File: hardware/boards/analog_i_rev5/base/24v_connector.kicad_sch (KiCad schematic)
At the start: 16 parts, among them IC8001 INA826AIDR, J8001 Barrel_Jack PJ-202BH, U4001 INA181A2

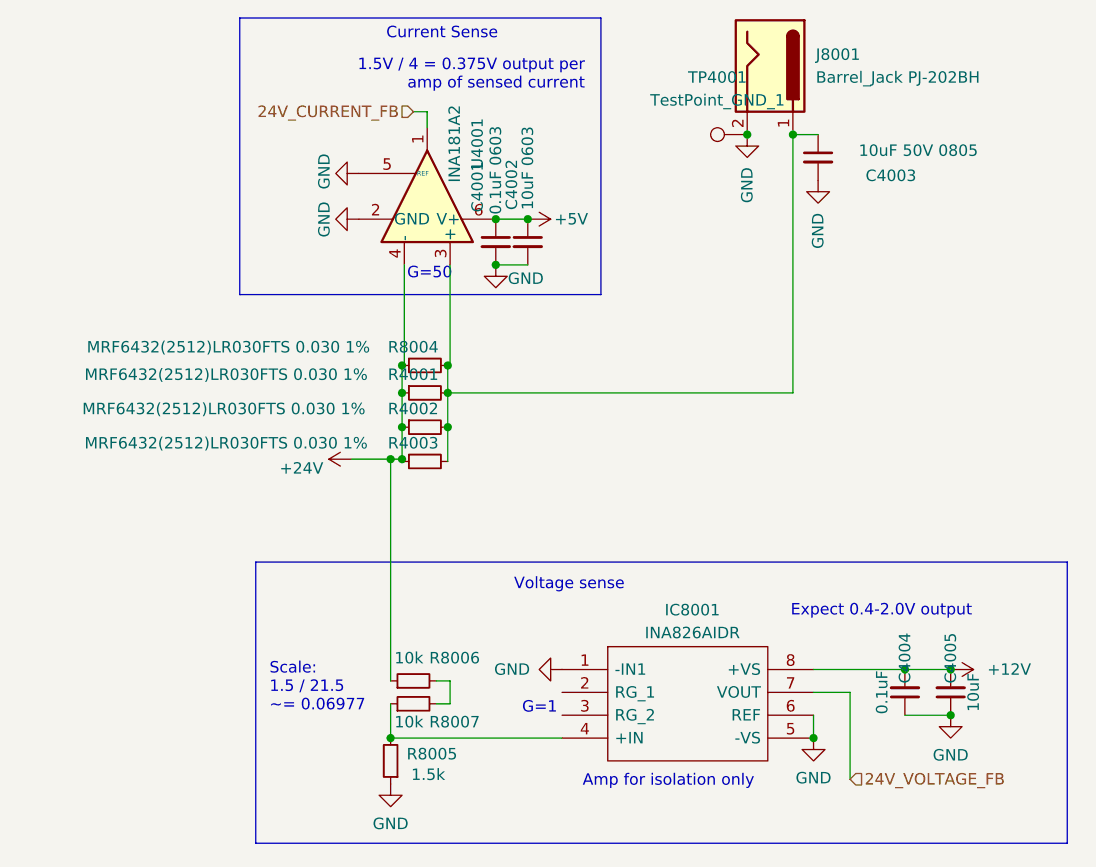
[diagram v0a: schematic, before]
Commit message: limit amp voltage outputs to 3.3V
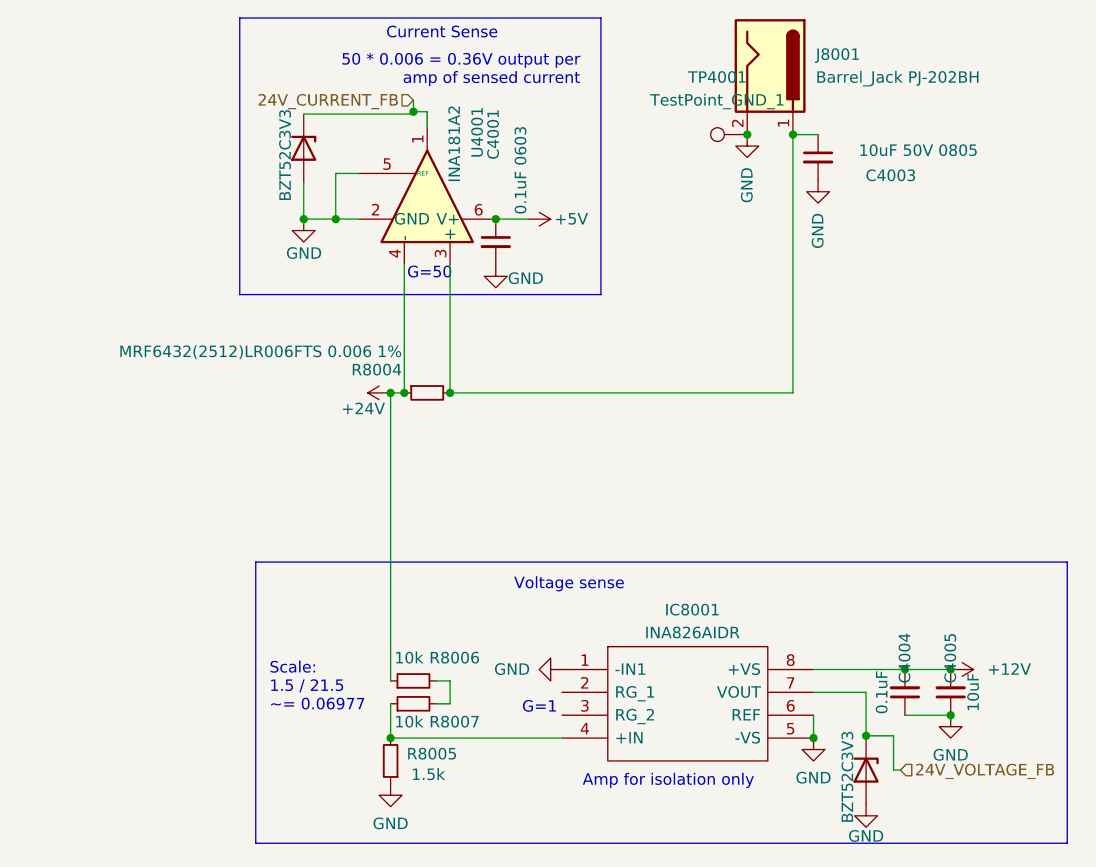
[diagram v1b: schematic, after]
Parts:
- removed C4002: 10uF 0603, Capacitor_SMD:C_0603_1608Metric, symbol Device:C_Small
- removed R4001, R4002, R4003: MRF6432(2512)LR030FTS 0.030 1%, Resistor_SMD:R_2512_6332Metric, symbol Device:R_Small
- added D5002, D5003: BZT52C3V3, Diode_SMD:D_SOD-323, symbol Device:D_Zener
- R8004: value MRF6432(2512)LR030FTS 0.030 1% -> MRF6432(2512)LR006FTS 0.006 1%; LCSC C76247 -> C76239
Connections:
- net 24V_CURRENT_FB: now also D5003.1 (K)
- net 24V_VOLTAGE_FB: now also D5002.1 (K)
- net GND: now also D5002.2 (A), D5003.2 (A)
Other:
- note added: "50 * 0.006 = 0.36V output per amp of sensed current"
- note removed: "1.5V / 4 = 0.375V output per amp of sensed current"
- note removed: "Expect 0.4-2.0V output"
- moved on the sheet: R8004

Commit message: update base layout
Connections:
- net +5V is gone; now on net +3V3: C4001.1, U4001.6 (V+)
- net +12V renamed +3V3
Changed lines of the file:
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@@
-	)
-	(junction
-		(at 140.462 150.622)
-		(diameter 0)
-		(color 0 0 0 0)
 	)
 	(junction
@@
 	(junction
 		(at 68.58 100.584)
+		(diameter 0)
+		(color 0 0 0 0)
+	)
+	(junction
+		(at 140.462 150.622)
 		(diameter 0)
 		(color 0 0 0 0)
@@
 	)
 	(symbol
-		(lib_id "power:+5V")
-		(at 93.472 100.584 270)
-		(mirror x)
+		(lib_id "power:+3V3")
+		(at 140.462 150.622 270)
 		(unit 1)
 		(exclude_from_sim no)
@@
 		(on_board yes)
 		(dnp no)
-		(property "Reference" "#PWR08005"
-			(at 89.662 100.584 0)
-			(effects
-				(font
-					(size 1.27 1.27)
-				)
-				(hide yes)
-			)
-		)
-		(property "Value" "+5V"
-			(at 98.298 100.584 90)
-			(effects
-				(font
-					(size 1.27 1.27)
-				)
+		(property "Reference" "#PWR4002"
+			(at 136.652 150.622 0)
+			(effects
+				(font
+					(size 1.27 1.27)
+				)
+				(hide yes)
+			)
+		)
+		(property "Value" "+3V3"
+			(at 143.256 150.368 90)
+			(effects
+				(font
+					(size 1.27 1.27)
+				)
+				(justify left)
 			)
 		)
 		(property "Footprint" ""
-			(at 93.472 100.584 0)
+			(at 140.462 150.622 0)
 			(effects
 				(font
@@
 		)
 		(property "Datasheet" ""
-			(at 93.472 100.584 0)
-			(effects
-				(font
-					(size 1.27 1.27)
-				)
-				(hide yes)
-			)
-		)
-		(property "Description" ""
-			(at 93.472 100.584 0)
+			(at 140.462 150.622 0)
+			(effects
+				(font
+					(size 1.27 1.27)
+				)
+				(hide yes)
+			)
+		)
+		(property "Description" "Power symbol creates a global label with name \"+3V3\""
+			(at 140.462 150.622 0)
 			(effects
 				(font
@@
 		)
 		(instances
-			(project ""
+			(project "stm32h7_base"
 				(path "/511605a4-f92c-43a6-a2c6-3cb535ac8a8e/0a1e0bd0-0a38-48a2-850f-3bdf02fef3ae"
-					(reference "#PWR08005")
-					(unit 1)
-				)
-			)
-			(project "simplicity_analog_1"
-				(path "/5a60c4b1-b6cb-416e-8883-8291fa089b87/b545dc42-87cf-45f6-8889-98202e5f492a/0a1e0bd0-0a38-48a2-850f-3bdf02fef3ae"
-					(reference "#PWR08005")
+					(reference "#PWR4002")
 					(unit 1)
 				)
@@
 		(dnp no)
 		(property "Reference" "C4005"
-			(at 140.462 149.352 90)
+			(at 140.462 146.812 90)
 			(effects
 				(font
@@
 		)
 		(property "Value" "10uF"
-			(at 143.002 153.162 90)
+			(at 143.002 154.178 90)
 			(effects
 				(font
@@
 		(dnp no)
 		(property "Reference" "C4004"
-			(at 135.382 149.352 90)
+			(at 135.382 146.812 90)
 			(effects
 				(font
@@
 				(path "/5a60c4b1-b6cb-416e-8883-8291fa089b87/b545dc42-87cf-45f6-8889-98202e5f492a/0a1e0bd0-0a38-48a2-850f-3bdf02fef3ae"
 					(reference "C8005")
+					(unit 1)
+				)
+			)
+		)
+	)
+	(symbol
+		(lib_id "power:+3V3")
+		(at 93.472 100.584 270)
+		(unit 1)
+		(exclude_from_sim no)
+		(in_bom yes)
+		(on_board yes)
+		(dnp no)
+		(property "Reference" "#PWR4003"
+			(at 89.662 100.584 0)
+			(effects
+				(font
+					(size 1.27 1.27)
+				)
+				(hide yes)
+			)
+		)
+		(property "Value" "+3V3"
+			(at 97.282 98.044 0)
+			(effects
+				(font
+					(size 1.27 1.27)
+				)
+				(justify left)
+			)
+		)
+		(property "Footprint" ""
+			(at 93.472 100.584 0)
+			(effects
+				(font
+					(size 1.27 1.27)
+				)
+				(hide yes)
+			)
+		)
+		(property "Datasheet" ""
+			(at 93.472 100.584 0)
+			(effects
+				(font
+					(size 1.27 1.27)
+				)
+				(hide yes)
+			)
+		)
+		(property "Description" "Power symbol creates a global label with name \"+3V3\""
+			(at 93.472 100.584 0)
+			(effects
+				(font
+					(size 1.27 1.27)
+				)
+				(hide yes)
+			)
+		)
+		(pin "1"
+		)
+		(instances
+			(project "stm32h7_base"
+				(path "/511605a4-f92c-43a6-a2c6-3cb535ac8a8e/0a1e0bd0-0a38-48a2-850f-3bdf02fef3ae"
+					(reference "#PWR4003")
 					(unit 1)
 				)
@@
 					(unit 1)
 				)
-			)
-		)
-	)
-	(symbol
-		(lib_id "power:+12V")
-		(at 140.462 150.622 270)
-		(unit 1)
-		(exclude_from_sim no)
-		(in_bom yes)
-		(on_board yes)
-		(dnp no)
-		(fields_autoplaced yes)
-		(property "Reference" "#PWR08009"
-			(at 136.652 150.622 0)
-			(effects
-				(font
-					(size 1.27 1.27)
-				)
-				(hide yes)
-			)
-		)
-		(property "Value" "+12V"
-			(at 144.526 150.6219 90)
-			(effects
-				(font
-					(size 1.27 1.27)
-				)
-				(justify left)
-			)
-		)
-		(property "Footprint" ""
-			(at 140.462 150.622 0)
-			(effects
-				(font
-					(size 1.27 1.27)
-				)
-				(hide yes)
-			)
-		)
-		(property "Datasheet" ""
-			(at 140.462 150.622 0)
-			(effects
-				(font
-					(size 1.27 1.27)
-				)
-				(hide yes)
-			)
-		)
-		(property "Description" ""
-			(at 140.462 150.622 0)
-			(effects
-				(font
-					(size 1.27 1.27)
-				)
-				(hide yes)
-			)
-		)
-		(pin "1"
-		)
-		(instances
-			(project ""
-				(path "/511605a4-f92c-43a6-a2c6-3cb535ac8a8e/0a1e0bd0-0a38-48a2-850f-3bdf02fef3ae"
-					(reference "#PWR08009")
-					(unit 1)
-				)
-			)
-			(project "simplicity_analog_1"
-				(path "/5a60c4b1-b6cb-416e-8883-8291fa089b87/b545dc42-87cf-45f6-8889-98202e5f492a/0a1e0bd0-0a38-48a2-850f-3bdf02fef3ae"
-					(reference "#PWR08009")
-					(unit 1)
-				)
